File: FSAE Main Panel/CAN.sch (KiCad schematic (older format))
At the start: 16 parts, among them U401 MCP25625, Y401 16MHz

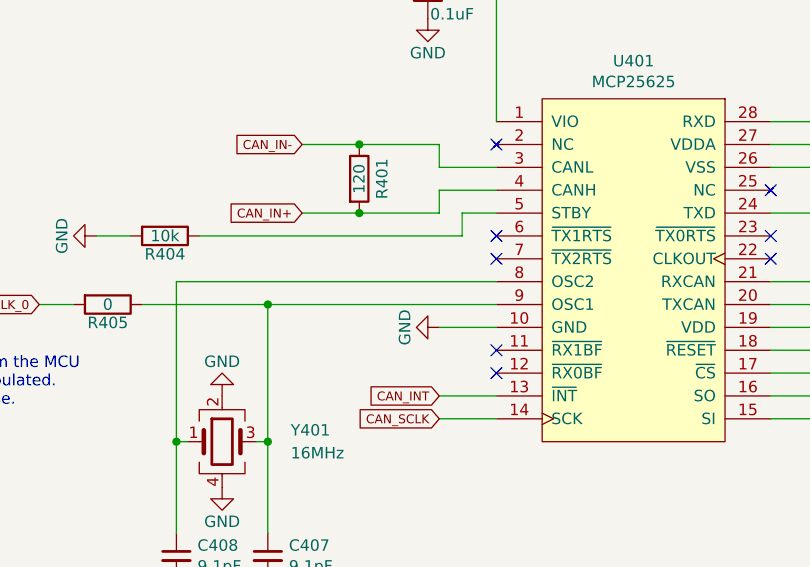
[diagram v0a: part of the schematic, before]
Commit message: Completed IO and CAN
Remaining: MCU pinning and changing the 3.3V supply locations
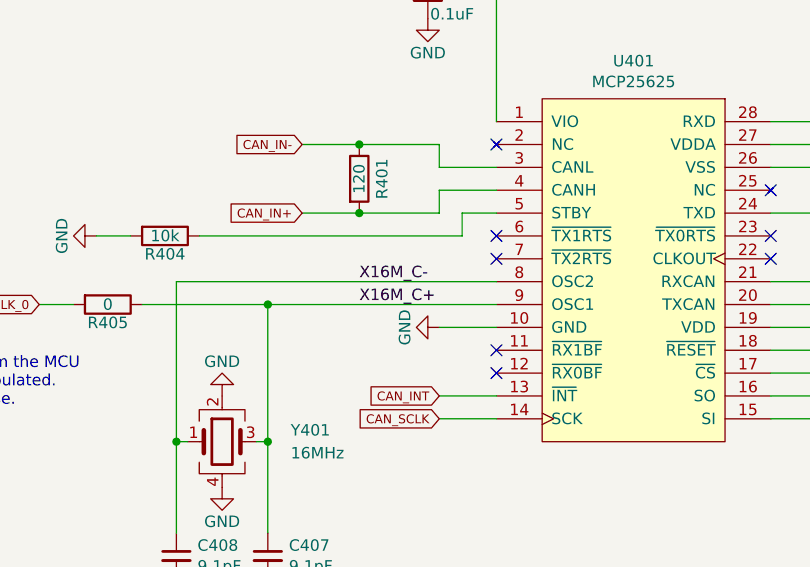
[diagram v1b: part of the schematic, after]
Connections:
- net X16M_C-: now reaches C408.1, U401.8 (OSC2), Y401.1
- net X16M_C+: now reaches C407.1, R405.1, U401.9 (OSC1), Y401.3
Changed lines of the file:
@@
 	7100 3150 7350 3150
 Connection ~ 7100 3150
+Text Label 4000 3650 0    50   ~ 0
+X16M_C+
+Text Label 4000 3550 0    50   ~ 0
+X16M_C-
 $EndSCHEMATC
